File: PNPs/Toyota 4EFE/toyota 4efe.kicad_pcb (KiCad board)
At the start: 4 copper layers, 92 parts, among them IC3 Trig Cond Socket, J1 Conn_01x02, J2 Conn_01x02, J9 4E-FE OEM, Q2 SSM3K357R, U1 VNLD5090, U2 IXDN602, U3 VNLD5090, U5 MPX4250, U6 SP720, U7 VNLD5090, U8 LM2940S-5.0/NOPB, U9 VNLD5090

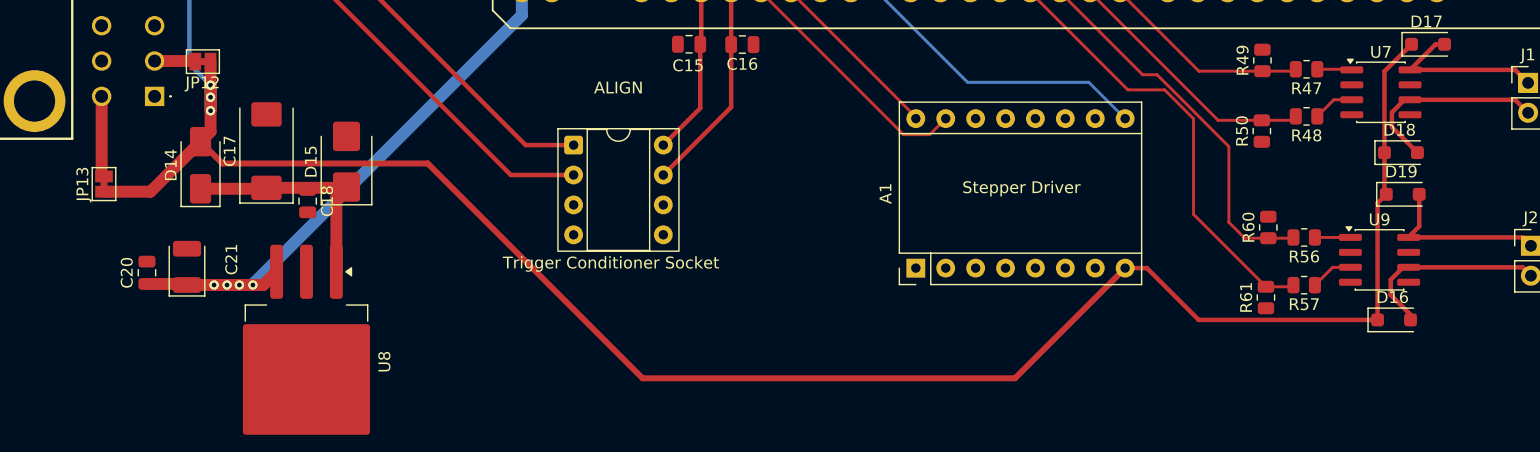
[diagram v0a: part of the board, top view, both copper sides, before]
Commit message: Small changes to silkscreen and part layout
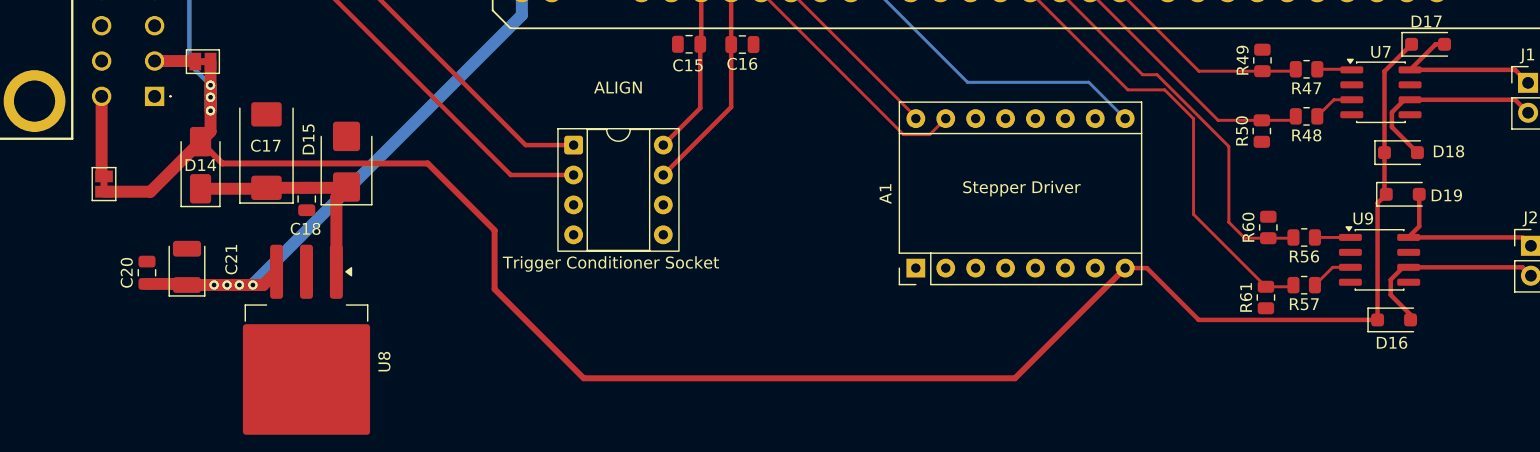
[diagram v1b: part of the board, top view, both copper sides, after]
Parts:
- moved C18 0.20 mm to (73.6, 132.6)
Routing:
- net 12V-SW: track 321.4 -> 324.3 mm
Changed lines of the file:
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@@
 		(tags "D_SOD-123F")
 		(property "Reference" "D16"
-			(at -0.127 -1.905 0)
+			(at -0.1925 1.98 0)
 			(layer "F.SilkS")
 			(effects
@@
 			(at 0 -1.8 0)
 			(layer "F.SilkS")
+			(hide yes)
 			(effects
 				(font
@@
 	(footprint "Capacitor_SMD:C_0805_2012Metric"
 		(layer "F.Cu")
-		(at 73.7 132.75 -90)
+		(at 73.62 132.57 -90)
 		(descr "Capacitor SMD 0805 (2012 Metric), square (rectangular) end terminal, IPC-7351 nominal, (Body size source: IPC-SM-782 page 76, https://www.pcb-3d.com/wordpress/wp-content/uploads/ipc-sm-782a_amendment_1_and_2.pdf, https://docs.google.com/spreadsheets/d/1BsfQQcO9C6DZCsRaXUlFlo91Tg2WpOkGARC1WS5S8t0/edit?usp=sharing), generated with kicad-footprint-generator")
 		(tags "capacitor")
 		(property "Reference" "C18"
-			(at 0 -1.68 90)
+			(at 2.57 0.09 180)
 			(layer "F.SilkS")
 			(effects
@@
 		(tags "D_SOD-123F")
 		(property "Reference" "D19"
-			(at -0.127 -1.905 0)
+			(at 3.7275 0.13 0)
 			(layer "F.SilkS")
 			(effects
@@
 		(tags "D_SOD-123F")
 		(property "Reference" "D18"
-			(at -0.127 -1.905 0)
+			(at 4.06 -0.07 0)
 			(layer "F.SilkS")
 			(effects
@@
 		(tags "SOIC SO")
 		(property "Reference" "U9"
-			(at 0 -3.4 0)
+			(at -1.39 -3.4775 0)
 			(layer "F.SilkS")
 			(effects
@@
 		(tags "capacitor tantalum")
 		(property "Reference" "C17"
-			(at 0 -3.1 90)
+			(at 0.42 -0.04 180)
 			(layer "F.SilkS")
 			(effects
@@
 		(tags "Diode SMB (DO-214AA)")
 		(property "Reference" "D15"
-			(at 0 -3 90)
+			(at 1.89 -3.19 270)
 			(layer "F.SilkS")
 			(effects
@@
 		(tags "Diode SMA (DO-214AC)")
 		(property "Reference" "D14"
-			(at 0 -2.5 90)
+			(at -0.0225 0 180)
 			(layer "F.SilkS")
 			(effects
@@
 			(at 0 -1.8 90)
 			(layer "F.SilkS")
+			(hide yes)
 			(effects
 				(font
@@
 	)
 	(segment
-		(start 66.45 129.55)
-		(end 83.9 129.55)
-		(width 0.508)
+		(start 131.3125 56.625)
+		(end 131.3125 53.6375)
+		(width 0.381)
 		(layer "F.Cu")
 		(net 1)
 	)
 	(segment
-		(start 131.3125 56.625)
-		(end 131.3125 53.6375)
-		(width 0.381)
+		(start 66.45 129.55)
+		(end 83.9 129.55)
+		(width 0.508)
 		(layer "F.Cu")
 		(net 1)
@@
 	)
 	(segment
+		(start 83.9 129.55)
+		(end 89.58 135.23)
+		(width 0.508)
+		(layer "F.Cu")
+		(net 1)
+	)
+	(segment
 		(start 65.45 125.075)
 		(end 65.45 126.85)
@@
 	)
 	(segment
-		(start 83.9 129.55)
-		(end 102.15 147.8)
+		(start 64.6 127.7)
+		(end 66.45 129.55)
 		(width 0.508)
 		(layer "F.Cu")
@@
 	)
 	(segment
-		(start 64.6 127.7)
-		(end 66.45 129.55)
-		(width 0.508)
-		(layer "F.Cu")
-		(net 1)
-	)
-	(segment
 		(start 165.17 121.73)
 		(end 165.17 128.63)
@@
 	)
 	(segment
-		(start 133.78 147.8)
-		(end 143.14 138.44)
+		(start 89.58 140.23)
+		(end 97.15 147.8)
 		(width 0.508)
 		(layer "F.Cu")
@@
 	)
 	(segment
-		(start 102.15 147.8)
+		(start 97.15 147.8)
 		(end 133.78 147.8)
 		(width 0.508)
@@
 	)
 	(segment
+		(start 133.78 147.8)
+		(end 143.14 138.44)
+		(width 0.508)
+		(layer "F.Cu")
+		(net 1)
+	)
+	(segment
 		(start 65.45 126.85)
 		(end 64.6 127.7)
@@
 		(layer "F.Cu")
 		(net 1)
+	)
+	(segment
+		(start 89.58 135.23)
+		(end 89.58 140.23)
+		(width 0.508)
+		(layer "F.Cu")
+		(net 1)

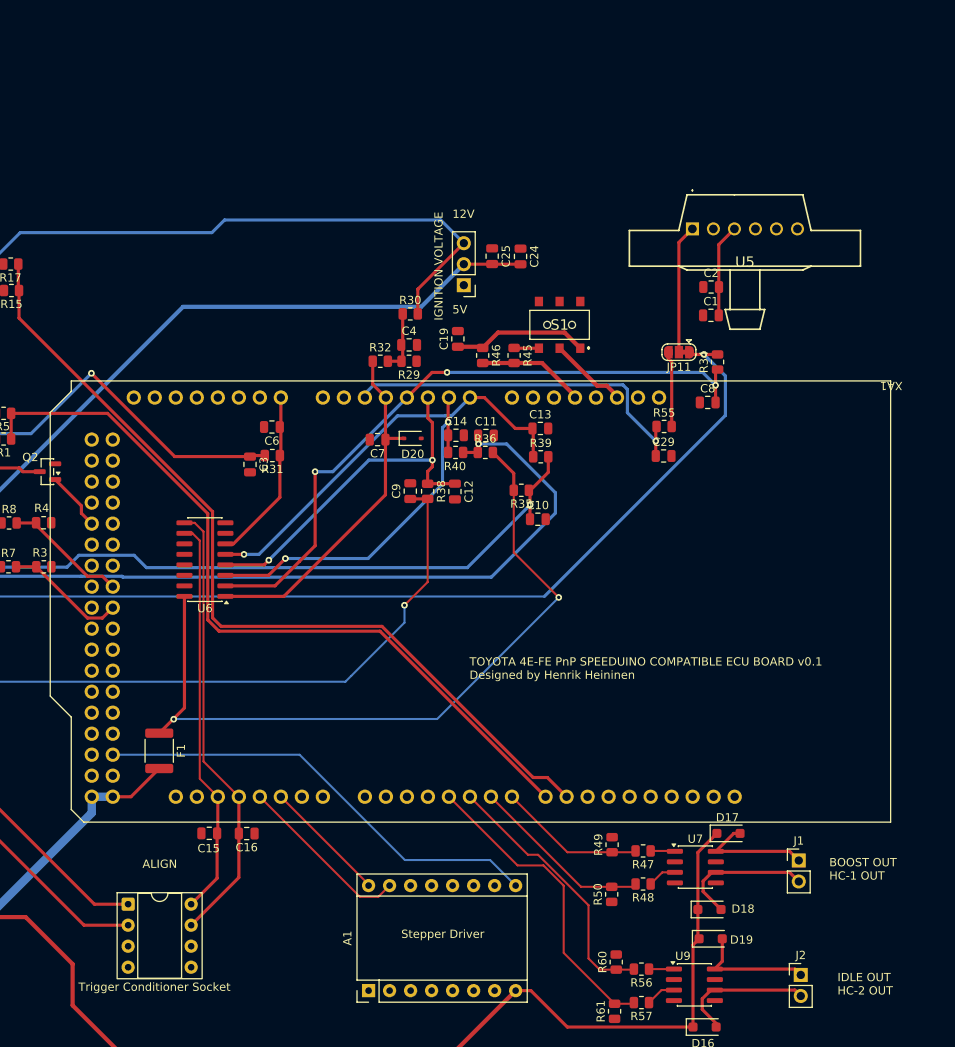
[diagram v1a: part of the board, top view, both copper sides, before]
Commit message: Added Mega shield, slight adjustments to traces
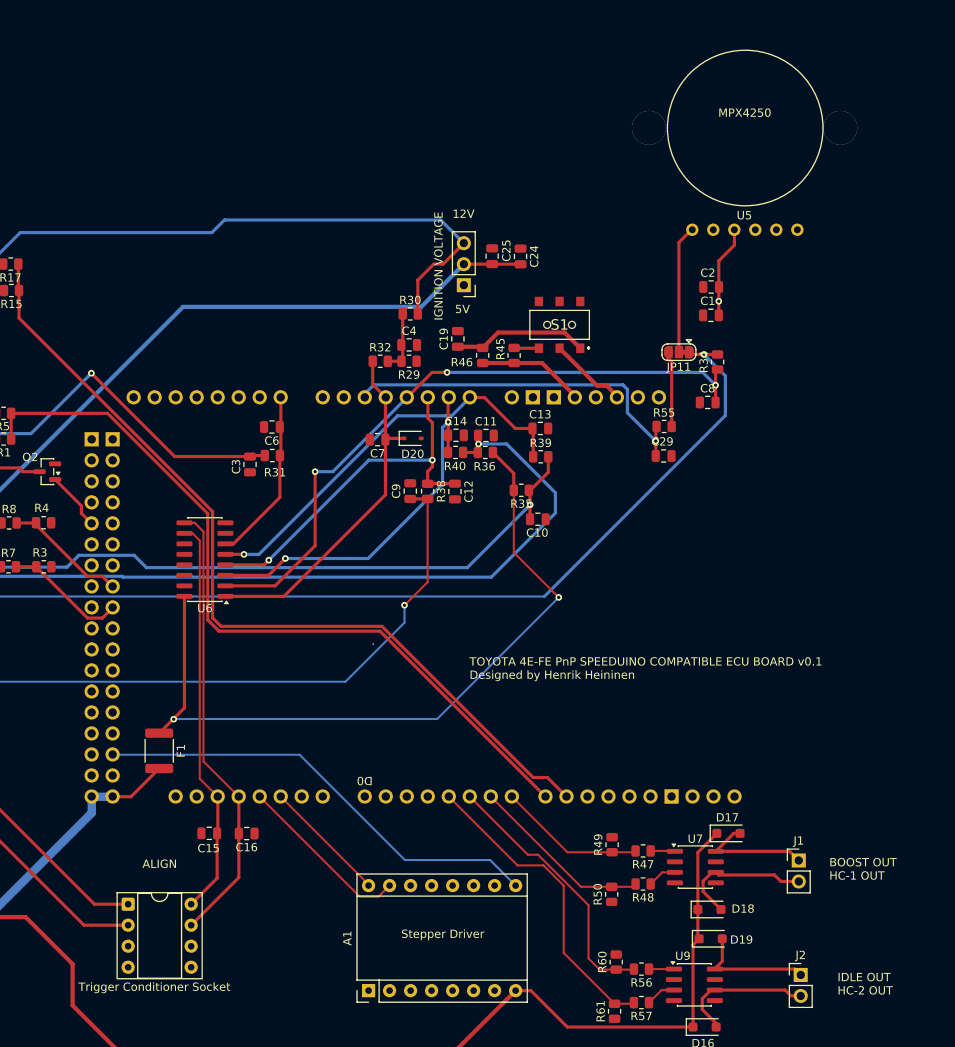
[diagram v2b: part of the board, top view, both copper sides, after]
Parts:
- U5: footprint Library:MPX5700ASX -> Misc:MPX4250
- XA1: footprint Library:Uno Shield -> Library:Arduino_Mega2560_R3_Shield
- moved XA1 54.5 mm to (188.4, 64.2)
- moved U5 0.10 mm to (164.5, 46.5)
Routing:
- net 12V-SW: track 324.3 -> 325.0 mm
- net VDD: vias 4 -> 5
